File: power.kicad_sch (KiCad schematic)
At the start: 35 parts, among them IC1 STUSB4531QTR, IC2 DCP3601NMR, IC3 BQ24810RUYR, J1 USB4230-03-A_REVA, Q1 SIR681DP-T1-RE3, Q2 SIR681DP-T1-RE3, U1 XSM6K519NW, U2 XSM6K519NW

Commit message: Ajout du BMS
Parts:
- removed C10, C8, C9: 100nF, Capacitor_SMD:C_0805_2012Metric, symbol local:C_0402
- removed C11: 1µF, Capacitor_SMD:C_0805_2012Metric, symbol local:C_0402
- removed C6: 42nF, Capacitor_SMD:C_0805_2012Metric, symbol local:C_0402
- removed C7: 1nF, Capacitor_SMD:C_0805_2012Metric, symbol local:C_0402
- removed IC3: BQ24810RUYR, local:QFN40P400X400X80-29N-D, symbol local:BQ24810RUYR
- removed J1: USB4230-03-A_REVA, local:GCT_USB4230-03-A_REVA, symbol local:USB4230-03-A_REVA
- removed R10, R9: 4k, Resistor_SMD:R_0805_2012Metric, symbol local:R
- removed R11: 866k, Resistor_SMD:R_0805_2012Metric, symbol local:R
- removed R12: 133k, Resistor_SMD:R_0805_2012Metric, symbol local:R
- removed R6: 0.001, Resistor_SMD:R_0805_2012Metric, symbol local:R
- removed R7, R8: 4.99, Resistor_SMD:R_0805_2012Metric, symbol local:R
- removed U1, U2: XSM6K519NW, local:DFN2020MD-6_SOT1220_NEX, symbol local:XSM6K519NW
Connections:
- net VBUS_A renamed VBUS_USB
- net V_SUB renamed V_BMS_IN
- no-connect marks 13 -> 3
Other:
- sheet BMS ports: added SCL, SDA, V_BMS_IN, V_BMS_OUT, ~{ALERT}; removed none
- note added: "BMS"
- note added: "V_SYS to 3.3V BUCK converter"
- note removed: "Near VCC IC3"
- note removed: "protection reverse ?"
- moved on the sheet: C1, C2, C200, C3, C4, C5, D4, IC1, IC2, L1, Q1, Q2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

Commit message: Update BMS
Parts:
- R4: value 47k -> 86.6k
- R5: value 47k -> 30k
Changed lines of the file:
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@@
 			)
 		)
-		(property "Value" "47k"
+		(property "Value" "86.6k"
 			(at 99.06 135.89 90)
 			(effects
@@
 			)
 		)
-		(property "Value" "47k"
+		(property "Value" "30k"
 			(at 92.71 140.97 90)
 			(effects

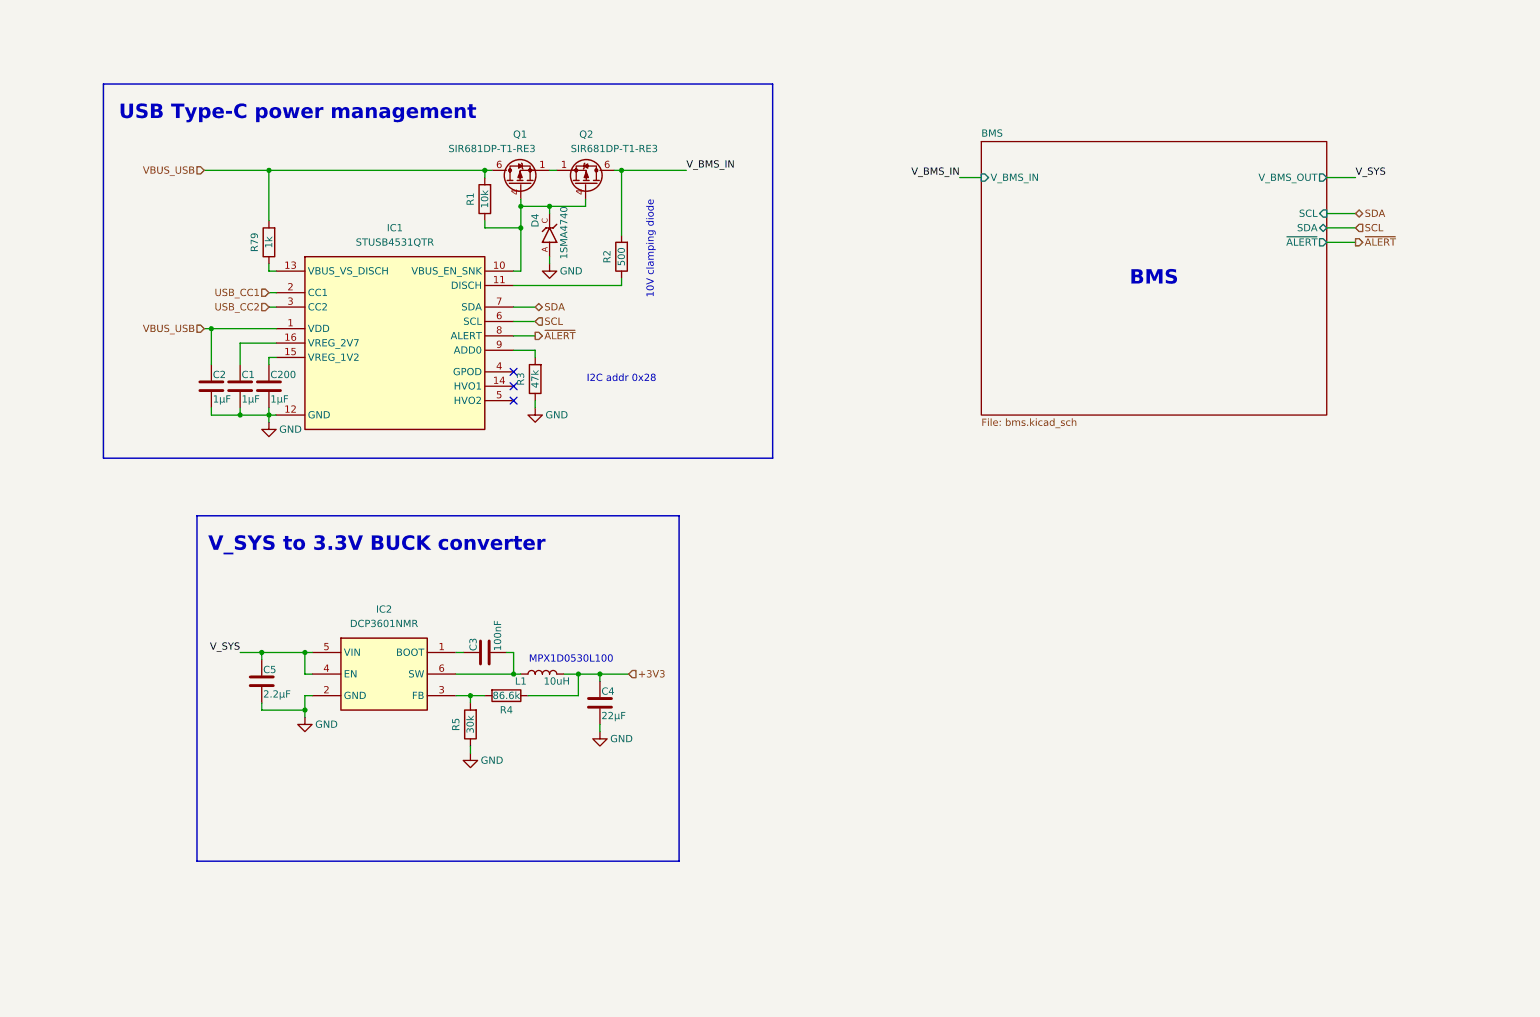
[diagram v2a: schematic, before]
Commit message: Version 0. Schémas finalisés. Mise à jour des résistances en série E12. Réduction de la BOM.
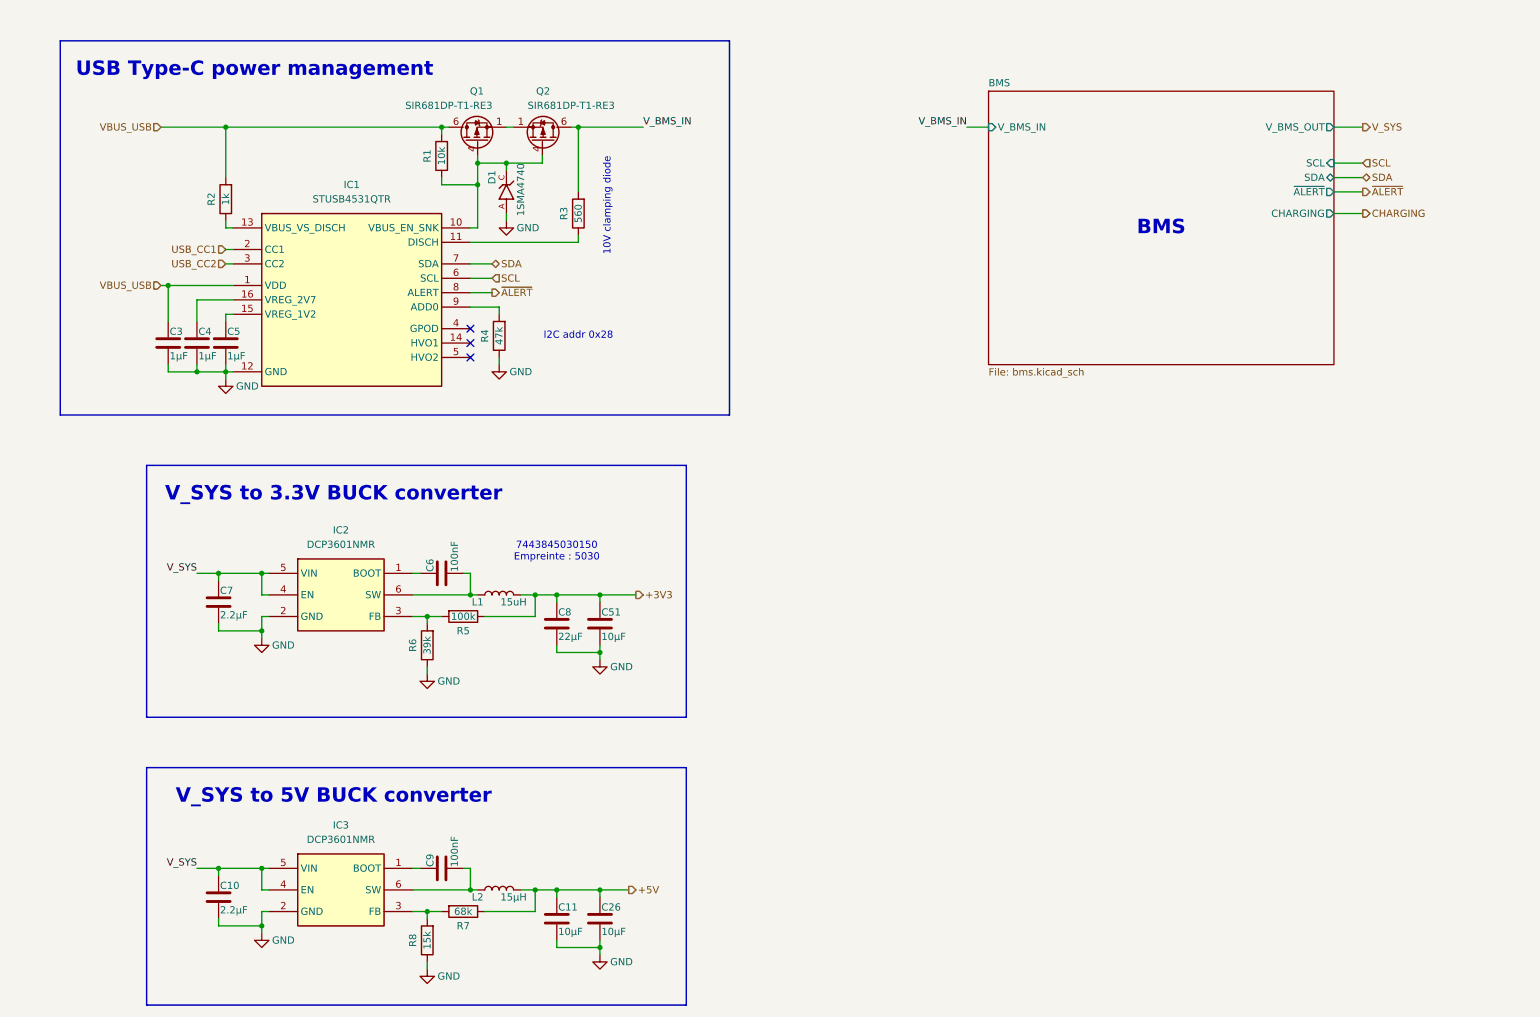
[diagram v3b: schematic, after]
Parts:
- added C10: 2.2µF, Capacitor_SMD:C_0805_2012Metric, symbol local:C_0402
- added C11, C26, C51: 10µF, Capacitor_SMD:C_0805_2012Metric, symbol local:C_0402
- added C9: 100nF, Capacitor_SMD:C_0805_2012Metric, symbol local:C_0402
- added IC3: DCP3601NMR, local:SOT95P280X125-6N, symbol local:DCP3601NMR
- added L2: 15µH, local:L_Wuerth_MAPI-5030, symbol Device:L
- added R7: 68k, Resistor_SMD:R_0805_2012Metric, symbol local:R
- added R8: 15k, Resistor_SMD:R_0805_2012Metric, symbol local:R
- L1: value 10uH -> 15uH; footprint (none) -> local:L_Wuerth_MAPI-5030
- R3: renamed from R2; value 500 -> 560
- R5: renamed from R4; value 86.6k -> 100k
- R6: renamed from R5; value 30k -> 39k
- renumbered C2 to C3, C1 to C4, C200 to C5, C3 to C6, C5 to C7, C4 to C8, D4 to D1, R79 to R2, R3 to R4
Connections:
- net +3V3: now also C51.1
- net GND: now also C10.2, C11.2, C26.2, C51.2, IC3.2 (GND), R8.1
- net V_SYS: now also C10.1, IC3.4 (EN), IC3.5 (VIN)
- new net: IC3.3 (FB), R7.2, R8.2
- new net: C9.1, IC3.1 (BOOT)
- new net: C9.2, IC3.6 (SW), L2.1
- new net +5V: C11.1, C26.1, L2.2, R7.1
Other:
- sheet BMS ports: added CHARGING; removed none
- note added: "7443845030150 Empreinte : 5030"
- note added: "V_SYS to 5V BUCK converter"
- note removed: "MPX1D0530L100"
- moved on the sheet: C3, C4, C5, C6, C7, C8, D1, IC1, IC2, L1, Q1, Q2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

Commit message: Minor Schematics update
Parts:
- removed Q1, Q2: SIR681DP-T1-RE3, local:SIR681DPT1RE3, symbol local:SIR681DP-T1-RE3
- added U12, U13: SQJ459EP-T2_BE3, local:SIJA54DPT1GE3, symbol local:SQJ459EP-T2_BE3
- C10: renamed from C9; footprint Capacitor_SMD:C_0805_2012Metric -> Capacitor_SMD:C_0603_1608Metric; symbol local:C_0402 -> local:C
- C11: renamed from C10; footprint Capacitor_SMD:C_0805_2012Metric -> Capacitor_SMD:C_0603_1608Metric; symbol local:C_0402 -> local:C
- C12: renamed from C11; symbol local:C_0402 -> local:C
- C13: renamed from C26; symbol local:C_0402 -> local:C
- C3, C4, C5, C6, C7: footprint Capacitor_SMD:C_0805_2012Metric -> Capacitor_SMD:C_0603_1608Metric; symbol local:C_0402 -> local:C
- C8: value 22µF -> 10µF; symbol local:C_0402 -> local:C
- C9: renamed from C51; symbol local:C_0402 -> local:C
- L1: value 15uH -> 15µH
- R10: renamed from R2; footprint Resistor_SMD:R_0805_2012Metric -> Resistor_SMD:R_0603_1608Metric
- R11: renamed from R3; footprint Resistor_SMD:R_0805_2012Metric -> Resistor_SMD:R_0603_1608Metric
- R12: renamed from R4; footprint Resistor_SMD:R_0805_2012Metric -> Resistor_SMD:R_0603_1608Metric
- R13: renamed from R5; footprint Resistor_SMD:R_0805_2012Metric -> Resistor_SMD:R_0603_1608Metric
- R14: renamed from R6; footprint Resistor_SMD:R_0805_2012Metric -> Resistor_SMD:R_0603_1608Metric
- R15: renamed from R7; footprint Resistor_SMD:R_0805_2012Metric -> Resistor_SMD:R_0603_1608Metric
- R16: renamed from R8; footprint Resistor_SMD:R_0805_2012Metric -> Resistor_SMD:R_0603_1608Metric
- R9: renamed from R1; footprint Resistor_SMD:R_0805_2012Metric -> Resistor_SMD:R_0603_1608Metric
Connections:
- net VBUS_USB: now also U13.D
- net V_BMS_IN: now also U12.D
- net at D1.C, IC1.10 (VBUS_EN_SNK), R9.1: now also U12.4, U13.4
- new net: U12.1, U12.2, U12.3, U13.1, U13.2, U13.3
